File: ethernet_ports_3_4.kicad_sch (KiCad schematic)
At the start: 15 parts, among them J3 JK0654219, J4 JK0654219, U1 KSZ9477S

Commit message: add TQFP-128_14x14mm_P0.4mm_EP10x10mm_ThermalVias footprint
and assign it to the ksz chip

Signed-off-by: Oleksij Rempel <linux@rempel-privat.de>
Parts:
- U1: footprint Package_QFP:TQFP-128_14x14mm_P0.4mm -> footprints:TQFP-128_14x14mm_P0.4mm_EP10x10mm_ThermalVias
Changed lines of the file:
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@@
     (property "Reference" "U1" (id 0) (at 38.1 27.94 0))
     (property "Value" "KSZ9477S" (id 1) (at 38.1 30.48 0))
-    (property "Footprint" "Package_QFP:TQFP-128_14x14mm_P0.4mm" (id 2) (at 20.066 69.342 0)
+    (property "Footprint" "footprints:TQFP-128_14x14mm_P0.4mm_EP10x10mm_ThermalVias" (id 2) (at 20.066 69.342 0)
       (effects (font (size 1.27 1.27)) hide)
     )
@@
     (property "Reference" "U1" (id 0) (at 38.1 129.54 0))
     (property "Value" "KSZ9477S" (id 1) (at 38.1 132.08 0))
-    (property "Footprint" "Package_QFP:TQFP-128_14x14mm_P0.4mm" (id 2) (at 20.066 170.942 0)
+    (property "Footprint" "footprints:TQFP-128_14x14mm_P0.4mm_EP10x10mm_ThermalVias" (id 2) (at 20.066 170.942 0)
       (effects (font (size 1.27 1.27)) hide)
     )

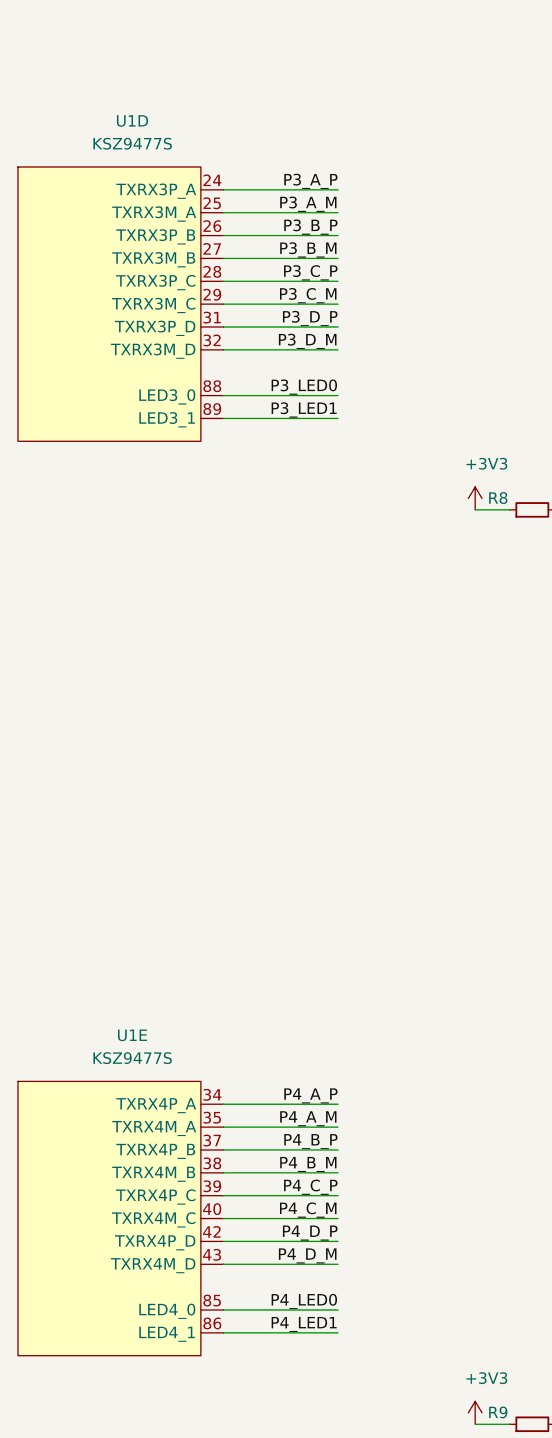
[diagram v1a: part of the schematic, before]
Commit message: update pin naming. use _P/_N to allow optiomisation for differential signal
Signed-off-by: Oleksij Rempel <linux@rempel-privat.de>
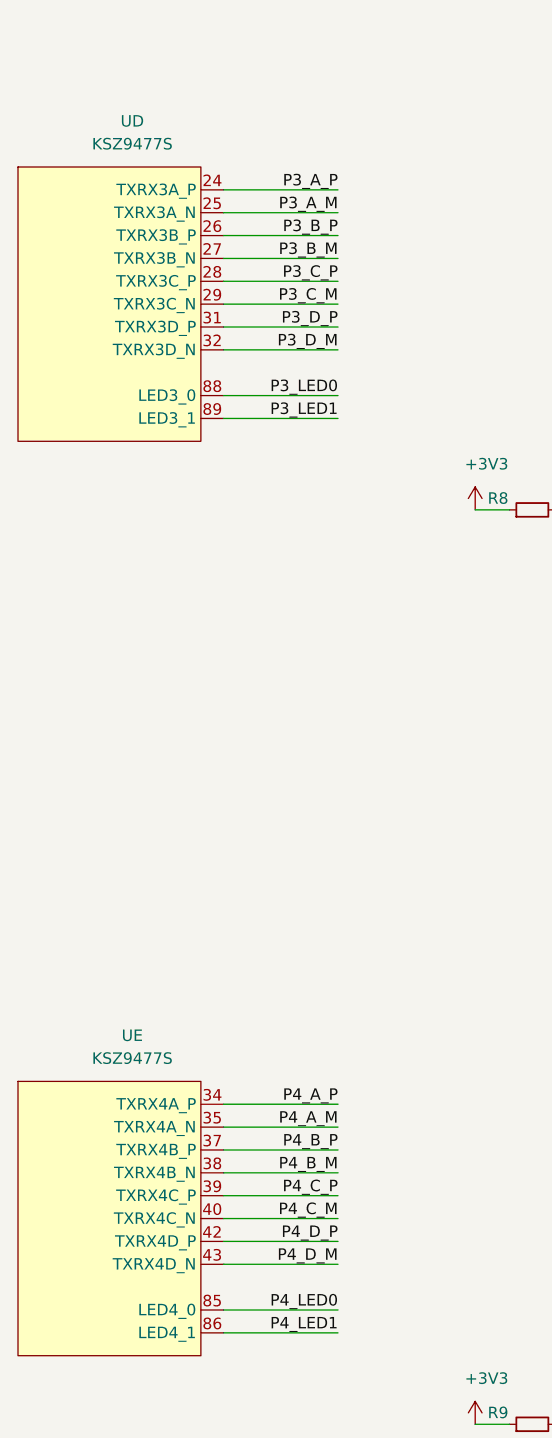
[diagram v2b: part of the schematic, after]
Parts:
- renumbered U1 to U
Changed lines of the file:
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@@
-(kicad_sch (version 20201015) (generator eeschema)
+(kicad_sch (version 20210126) (generator eeschema)
   (paper "A4")
   (junction (at 92.71 43.18) (diameter 0.9144) (color 0 0 0 0))
@@
       (effects (font (size 1.27 1.27)) hide)
     )
+    (pin "1")
   )
   (symbol (lib_id "power:+3V3") (at 76.2 172.72 0) (unit 1)
@@
       (effects (font (size 1.27 1.27)) hide)
     )
+    (pin "1")
   )
   (symbol (lib_id "power:+3V3") (at 91.44 22.86 0) (unit 1)
@@
       (effects (font (size 1.27 1.27)) hide)
     )
+    (pin "1")
   )
   (symbol (lib_id "power:+3V3") (at 91.44 124.46 0) (unit 1)
@@
       (effects (font (size 1.27 1.27)) hide)
     )
+    (pin "1")
   )
   (symbol (lib_id "power:GND") (at 92.71 63.5 0) (unit 1)
@@
       (effects (font (size 1.27 1.27)) hide)
     )
+    (pin "1")
   )
   (symbol (lib_id "power:GND") (at 92.71 165.1 0) (unit 1)
@@
       (effects (font (size 1.27 1.27)) hide)
     )
+    (pin "1")
   )
   (symbol (lib_id "power:Earth") (at 137.16 78.74 0) (unit 1)
@@
       (effects (font (size 1.27 1.27)) hide)
     )
+    (pin "1")
   )
   (symbol (lib_id "power:Earth") (at 137.16 180.34 0) (unit 1)
@@
       (effects (font (size 1.27 1.27)) hide)
     )
+    (pin "1")
   )
   (symbol (lib_id "Device:R_Small") (at 82.55 71.12 90) (unit 1)
@@
       (effects (font (size 1.27 1.27)) hide)
     )
+    (pin "1")
+    (pin "2")
   )
   (symbol (lib_id "Device:R_Small") (at 82.55 172.72 90) (unit 1)
@@
       (effects (font (size 1.27 1.27)) hide)
     )
+    (pin "1")
+    (pin "2")
   )
   (symbol (lib_id "Device:R_Small") (at 97.79 22.86 90) (unit 1)
@@
       (effects (font (size 1.27 1.27)) hide)
     )
+    (pin "1")
+    (pin "2")
   )
   (symbol (lib_id "Device:R_Small") (at 97.79 124.46 90) (unit 1)
@@
       (effects (font (size 1.27 1.27)) hide)
     )
+    (pin "1")
+    (pin "2")
   )
   (symbol (lib_id "Device:C_Small") (at 97.79 33.02 270) (unit 1)
@@
       (effects (font (size 1.27 1.27)) hide)
     )
+    (pin "1")
+    (pin "2")
   )
   (symbol (lib_id "Device:C_Small") (at 97.79 43.18 270) (unit 1)
@@
       (effects (font (size 1.27 1.27)) hide)
     )
+    (pin "1")
+    (pin "2")
   )
   (symbol (lib_id "Device:C_Small") (at 97.79 53.34 270) (unit 1)
@@
       (effects (font (size 1.27 1.27)) hide)
     )
+    (pin "1")
+    (pin "2")
   )
   (symbol (lib_id "Device:C_Small") (at 97.79 63.5 270) (unit 1)
@@
       (effects (font (size 1.27 1.27)) hide)
     )
+    (pin "1")
+    (pin "2")
   )
   (symbol (lib_id "Device:C_Small") (at 97.79 134.62 270) (unit 1)
@@
       (effects (font (size 1.27 1.27)) hide)
     )
+    (pin "1")
+    (pin "2")
   )
   (symbol (lib_id "Device:C_Small") (at 97.79 144.78 270) (unit 1)
@@
       (effects (font (size 1.27 1.27)) hide)
     )
+    (pin "1")
+    (pin "2")
   )
   (symbol (lib_id "Device:C_Small") (at 97.79 154.94 270) (unit 1)
@@
       (effects (font (size 1.27 1.27)) hide)
     )
+    (pin "1")
+    (pin "2")
   )
   (symbol (lib_id "Device:C_Small") (at 97.79 165.1 270) (unit 1)
@@
       (effects (font (size 1.27 1.27)) hide)
     )
-  )
-  (symbol (lib_id "local:KSZ9477S") (at 35.56 48.26 0) (unit 4)
-    (in_bom yes) (on_board yes)
-    (property "Reference" "U1" (id 0) (at 38.1 27.94 0))
+    (pin "1")
+    (pin "2")
+  )
+  (symbol (lib_name "local:KSZ9477S_1") (lib_id "local:KSZ9477S") (at 35.56 48.26 0) (unit 4)
+    (in_bom yes) (on_board yes)
+    (property "Reference" "U" (id 0) (at 38.1 27.94 0))
     (property "Value" "KSZ9477S" (id 1) (at 38.1 30.48 0))
     (property "Footprint" "footprints:TQFP-128_14x14mm_P0.4mm_EP10x10mm_ThermalVias" (id 2) (at 20.066 69.342 0)
@@
       (effects (font (size 1.27 1.27)) hide)
     )
+    (pin "26")
+    (pin "27")
+    (pin "28")
+    (pin "29")
+    (pin "31")
+    (pin "24")
+    (pin "25")
+    (pin "32")
+    (pin "88")
+    (pin "89")
   )
   (symbol (lib_id "local:KSZ9477S") (at 35.56 149.86 0) (unit 5)
     (in_bom yes) (on_board yes)
-    (property "Reference" "U1" (id 0) (at 38.1 129.54 0))
+    (property "Reference" "U" (id 0) (at 38.1 129.54 0))
     (property "Value" "KSZ9477S" (id 1) (at 38.1 132.08 0))
     (property "Footprint" "footprints:TQFP-128_14x14mm_P0.4mm_EP10x10mm_ThermalVias" (id 2) (at 20.066 170.942 0)
@@
       (effects (font (size 1.27 1.27)) hide)
     )
+    (pin "37")
+    (pin "38")
+    (pin "39")
+    (pin "40")
+    (pin "42")
+    (pin "34")
+    (pin "35")
+    (pin "43")
+    (pin "85")
+    (pin "86")
   )
   (symbol (lib_id "Connector:JK0654219") (at 137.16 48.26 0) (unit 1)
@@
       (effects (font (size 1.27 1.27)) hide)
     )
+    (pin "1")
+    (pin "10")
+    (pin "11")
+    (pin "12")
+    (pin "13")
+    (pin "14")
+    (pin "15")
+    (pin "16")
+    (pin "2")
+    (pin "3")
+    (pin "4")
+    (pin "5")
+    (pin "6")
+    (pin "7")
+    (pin "8")
+    (pin "9")
+    (pin "SH")
   )
   (symbol (lib_id "Connector:JK0654219") (at 137.16 149.86 0) (unit 1)
@@
       (effects (font (size 1.27 1.27)) hide)
     )
+    (pin "1")
+    (pin "10")
+    (pin "11")
+    (pin "12")
+    (pin "13")
+    (pin "14")
+    (pin "15")
+    (pin "16")
+    (pin "2")
+    (pin "3")
+    (pin "4")
+    (pin "5")
+    (pin "6")
+    (pin "7")
+    (pin "8")
+    (pin "9")
+    (pin "SH")
   )
 )
